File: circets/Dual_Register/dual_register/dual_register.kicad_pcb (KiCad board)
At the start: 2 copper layers, 110 x 162 mm, 13 parts, among them J1 Bus_Connector, J2 D_H, J3 D_L, J4 Conn_01x03_Male, U1 AM-Connector, U2 74HC573, U3 74HC573, U4 74HC573, U5 74HC573, U6 74HC573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

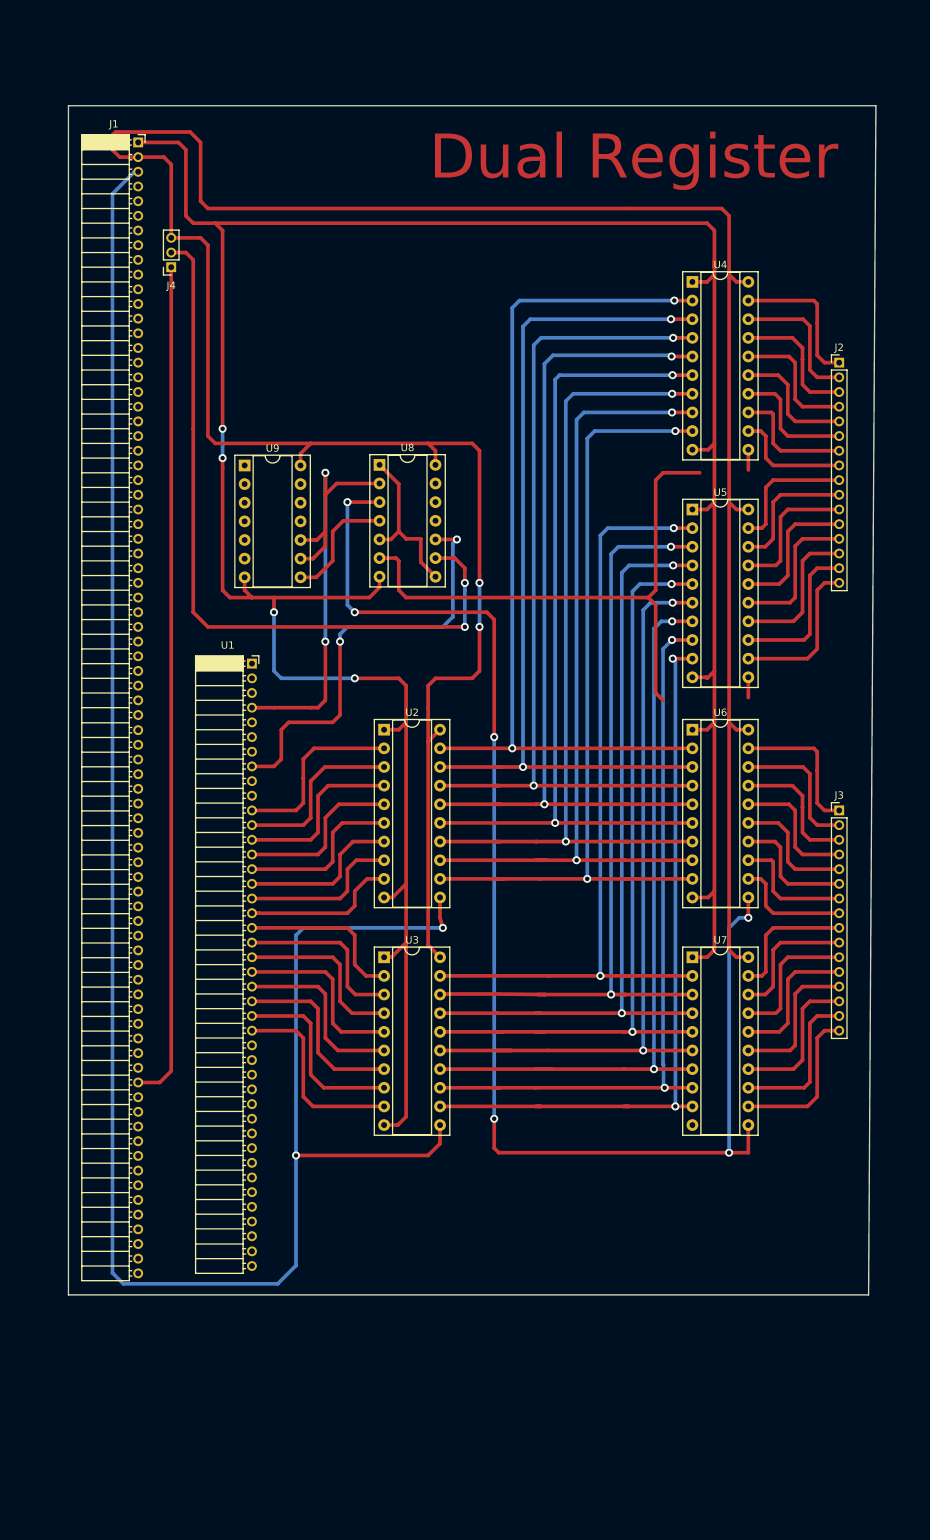
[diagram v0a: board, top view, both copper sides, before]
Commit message: Enlarge Via Size
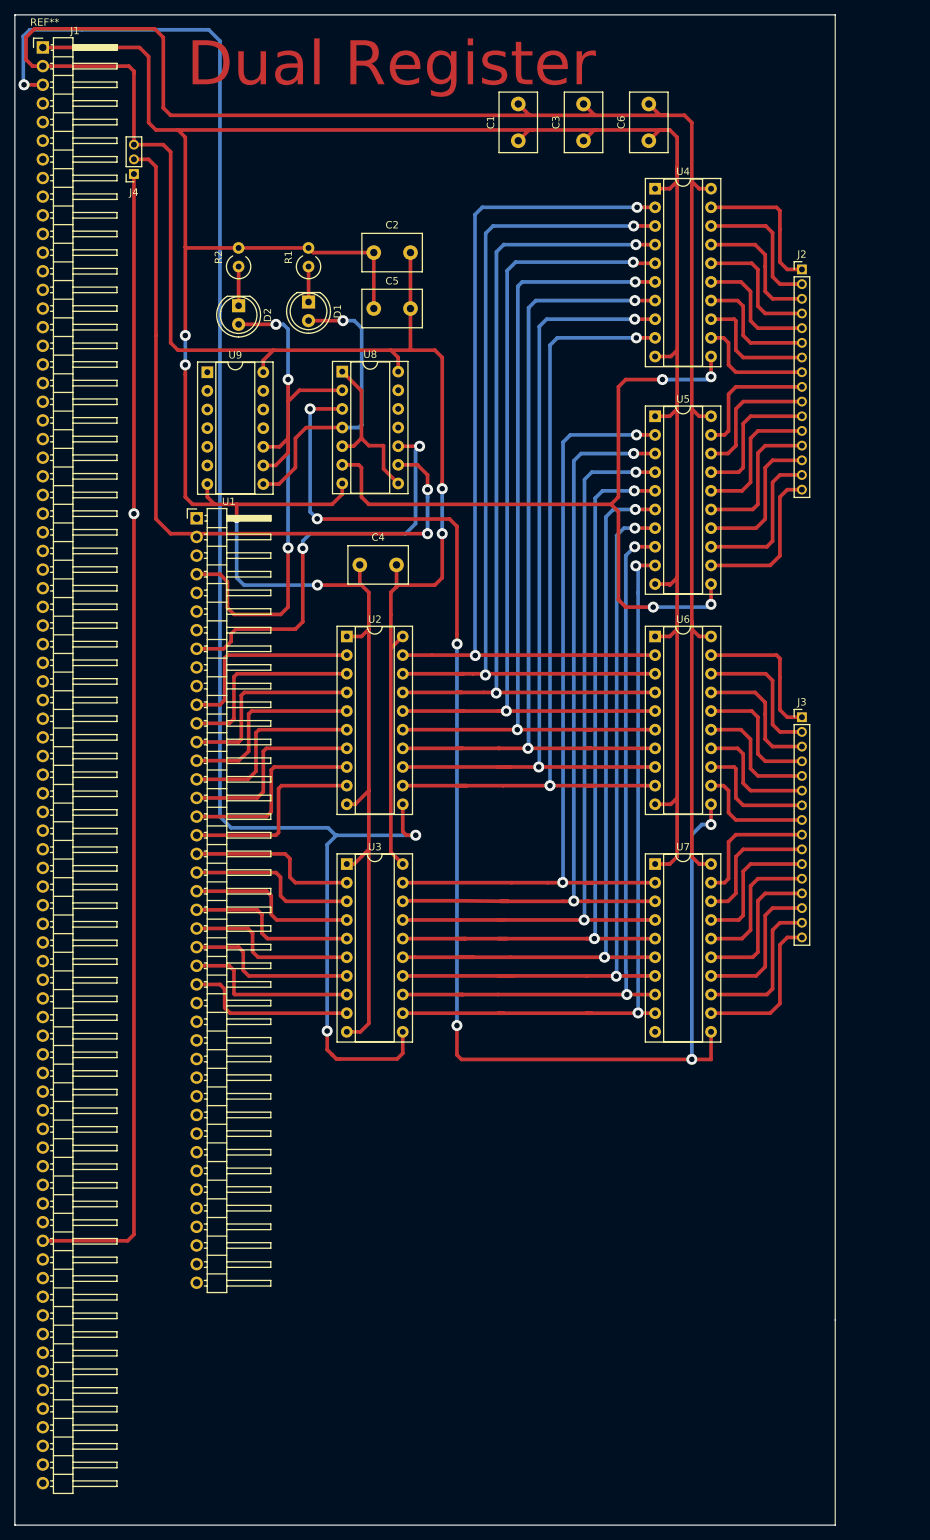
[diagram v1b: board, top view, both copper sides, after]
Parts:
- added C1: 0.1µF, Capacitor_THT:C_Disc_D8.0mm_W5.0mm_P5.00mm, F.Cu at (81.3, 24.8)
- added C2: 0.1µF, Capacitor_THT:C_Disc_D8.0mm_W5.0mm_P5.00mm, F.Cu at (61.6, 40.0)
- added C3: 0.1µF, Capacitor_THT:C_Disc_D8.0mm_W5.0mm_P5.00mm, F.Cu at (90.2, 24.8)
- added C4: 0.1µF, Capacitor_THT:C_Disc_D8.0mm_W5.0mm_P5.00mm, F.Cu at (59.7, 82.5)
- added C5: 0.1µF, Capacitor_THT:C_Disc_D8.0mm_W5.0mm_P5.00mm, F.Cu at (61.6, 47.6)
- added C6: 0.1µF, Capacitor_THT:C_Disc_D8.0mm_W5.0mm_P5.00mm, F.Cu at (99.1, 24.8)
- added D1: LED, LED_THT:LED_D5.0mm, F.Cu at (52.7, 46.7)
- added D2: LED, LED_THT:LED_D5.0mm, F.Cu at (43.2, 47.2)
- added R1: 220, Resistor_THT:R_Axial_DIN0309_L9.0mm_D3.2mm_P2.54mm_Vertical, F.Cu at (52.7, 41.9)
- added R2: 220, Resistor_THT:R_Axial_DIN0309_L9.0mm_D3.2mm_P2.54mm_Vertical, F.Cu at (43.2, 41.9)
- J1: footprint Computer_Component_Library:PinSocket_1x78_P2.00mm_Horizontal -> Computer_Component_Library:PinHeader_1x78_P2.54mm_Horizontal
- U1: footprint Computer_Component_Library:PinSocket_1x42_P2.00mm_Horizontal -> Computer_Component_Library:PinHeader_1x42_P2.54mm_Horizontal
- moved U1 21.2 mm to (37.5, 76.2)
- moved J1 18.3 mm to (16.5, 12.1)
- moved U8 13.7 mm to (57.3, 56.2)
- moved J2 13.7 mm to (119.9, 42.3)
- moved J3 13.7 mm to (119.9, 103.3)
- moved U2 13.7 mm to (57.9, 92.3)
- moved U3 13.7 mm to (57.9, 123.3)
- moved U5 13.7 mm to (99.9, 62.3)
- moved U6 13.7 mm to (99.9, 92.3)
- moved U7 13.7 mm to (99.9, 123.3)
- moved U9 13.7 mm to (38.9, 56.3)
- moved J4 13.7 mm to (28.9, 29.3)
- moved U4 13.7 mm to (99.9, 31.3)
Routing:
- net GND: track 391.0 -> 443.8 mm
- net Net-(J1-Pad3): track 270.8 -> 220.0 mm, vias 2 -> 3
- net Net-(J1-Pad65): track 114.6 -> 157.2 mm, vias 0 -> 1
- net +5V: track 381.5 -> 421.2 mm
- net Net-(D1-Pad2): track 16.3 -> 39.9 mm, vias 0 -> 1
- net Net-(D2-Pad2): track 67.4 -> 88.1 mm, vias 2 -> 3
- net Net-(U4-Pad11): track 84.4 -> 103.0 mm, vias 0 -> 4
- net Net-(U1-Pad18): track 21.1 -> 26.8 mm
- net Net-(D2-Pad1): track 0.00 -> 5.08 mm
- net Net-(D1-Pad1): track 0.00 -> 4.83 mm
- net Net-(U1-Pad17): track 21.9 -> 26.6 mm
- net Net-(U1-Pad16): track 22.1 -> 26.5 mm
- net Net-(U1-Pad26): track 27.0 -> 23.6 mm
- net Net-(U1-Pad15): track 23.0 -> 26.3 mm
- net Net-(U1-Pad14): track 23.2 -> 26.2 mm
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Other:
- board size 110 x 162 mm -> 111.8 x 205.7 mm
- net class Default: via_dia 1.1 -> 1.5; via_drill 0.6 -> 0.75
- rule via_min_drill: 0.6 -> 0.5
- rule via_min_size: 0.6 -> 1
